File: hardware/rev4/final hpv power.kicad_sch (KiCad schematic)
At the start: 27 parts, among them J1 Conn_02x03_Odd_Even, J2 Conn_01x04_Pin, Q1 PNP, U1 ESP32-S3-MINI-1, U2 MCP1825S, U3 HX711

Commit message: fixed up things for justin to look
fixed up things for justin to look
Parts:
- removed J1: Conn_02x03_Odd_Even, Connector_IDC:IDC-Header_2x03_P2.54mm_Vertical, symbol Connector_Generic:Conn_02x03_Odd_Even
- added J3: USB_C_Receptacle_USB2.0_14P, Connector_USB:USB_C_Receptacle_GCT_USB4110, symbol Connector:USB_C_Receptacle_USB2.0_14P
- added R7, R8: 5.1k, Resistor_SMD:R_0805_2012Metric, symbol Device:R
- C1, C10, C11, C12, C2, C3, C4, C5, C6, C7, C8, C9: footprint Capacitor_SMD:C_0603_1608Metric -> Capacitor_SMD:C_0805_2012Metric
- D1, D2: footprint LED_SMD:LED_0603_1608Metric -> LED_SMD:LED_0805_2012Metric
- R1, R2, R3, R4, R5, R6: footprint Resistor_SMD:R_0603_1608Metric -> Resistor_SMD:R_0805_2012Metric
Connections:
- net BATT: no longer C5.2, U2.1 (VI)
- net GND: now also J3.A1 (GND), J3.A12 (GND), J3.B1 (GND), J3.B12 (GND), J3.S1 (SHIELD), R7.2, R8.2
- net D-: now reaches U1.23 (USB_D-)
- net D-: now also J3.A7 (D-), J3.B7 (D-)
- net D+: now reaches U1.24 (USB_D+)
- net D+: now also J3.A6 (D+), J3.B6 (D+)
- net RX: no longer names the net of U1.40 (RXD0)
- net TX: no longer names the net of U1.39 (TXD0)
- new net: J3.A5 (CC1), R7.1
- new net: J3.B5 (CC2), R8.1
- new net VBUS: C5.2, J3.A4 (VBUS), J3.A9 (VBUS), J3.B4 (VBUS), J3.B9 (VBUS), U2.1 (VI)
- no-connect marks 31 -> 29
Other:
- note removed: "Can look into an external analog digital converter, apparently the one in the mcu isnt very precise for the strain gauge signals we are reading"
- note removed: "Figure out bluetooth low energy, and battery"
- note removed: "Need to check pinouts for mcu Clear Errors Look into USBC"
- note removed: "Noah: battery should be pretty simple, connect to voltage reg according to datasheet bluetooth low energy is built into the MCU, we just have to code it with the right library"
- note removed: "Programming (ESP PROG)"
- note removed: "eason"

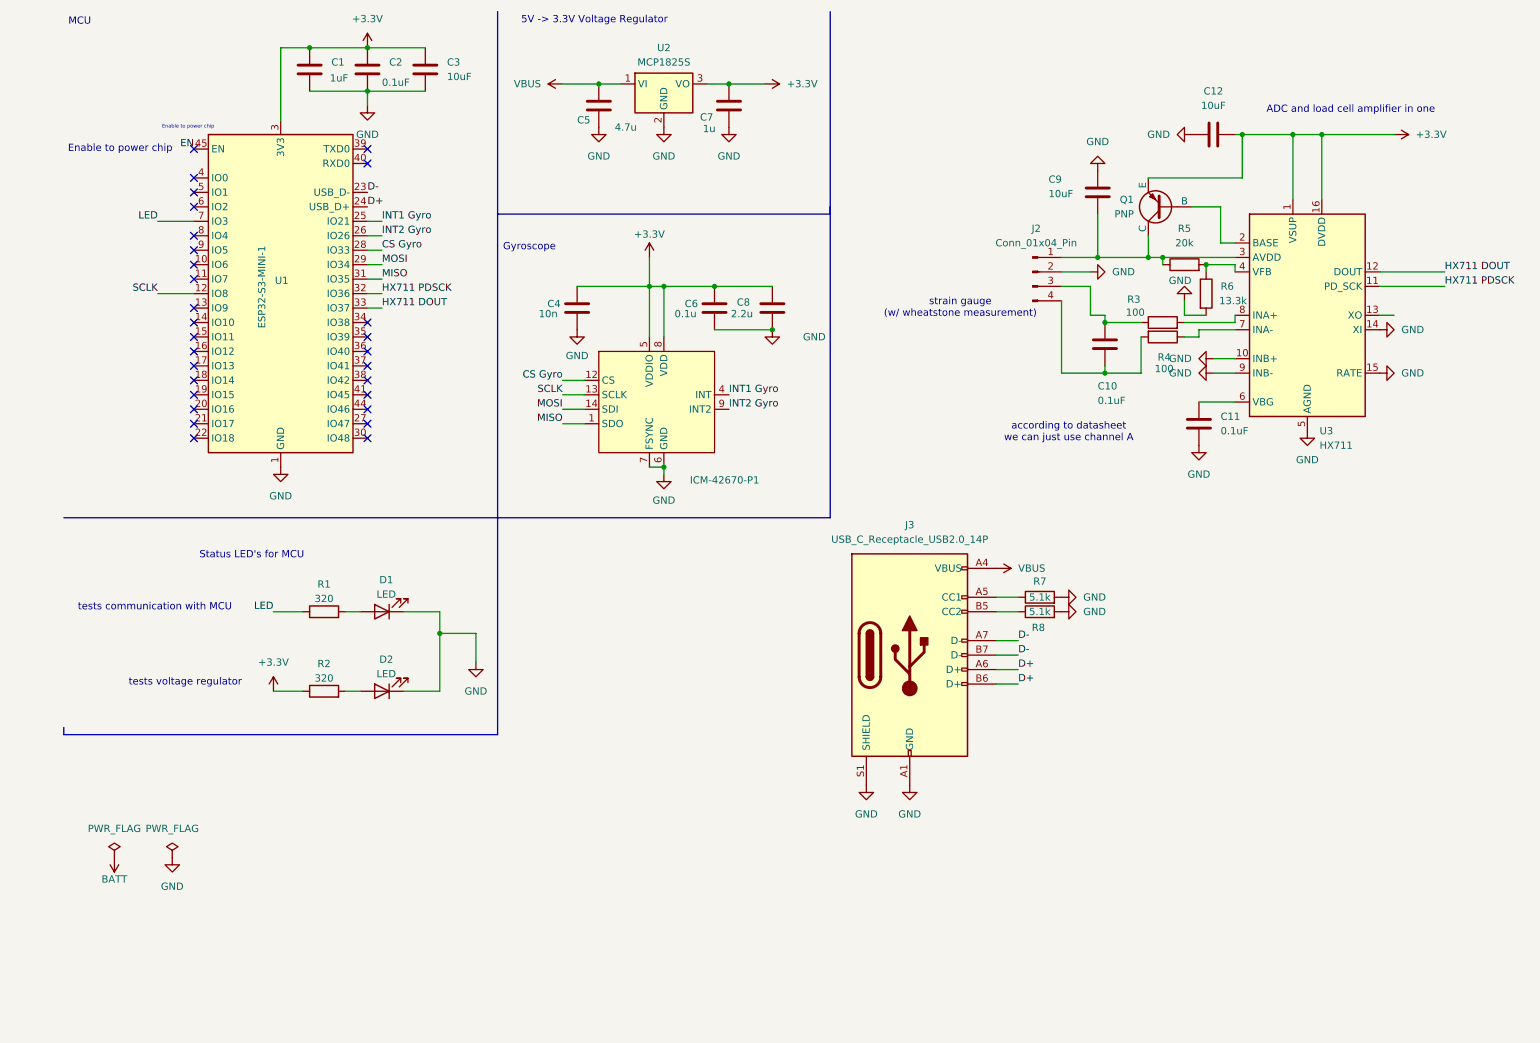
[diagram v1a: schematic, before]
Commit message: Fixed schematic based on Noah's notes from Justin
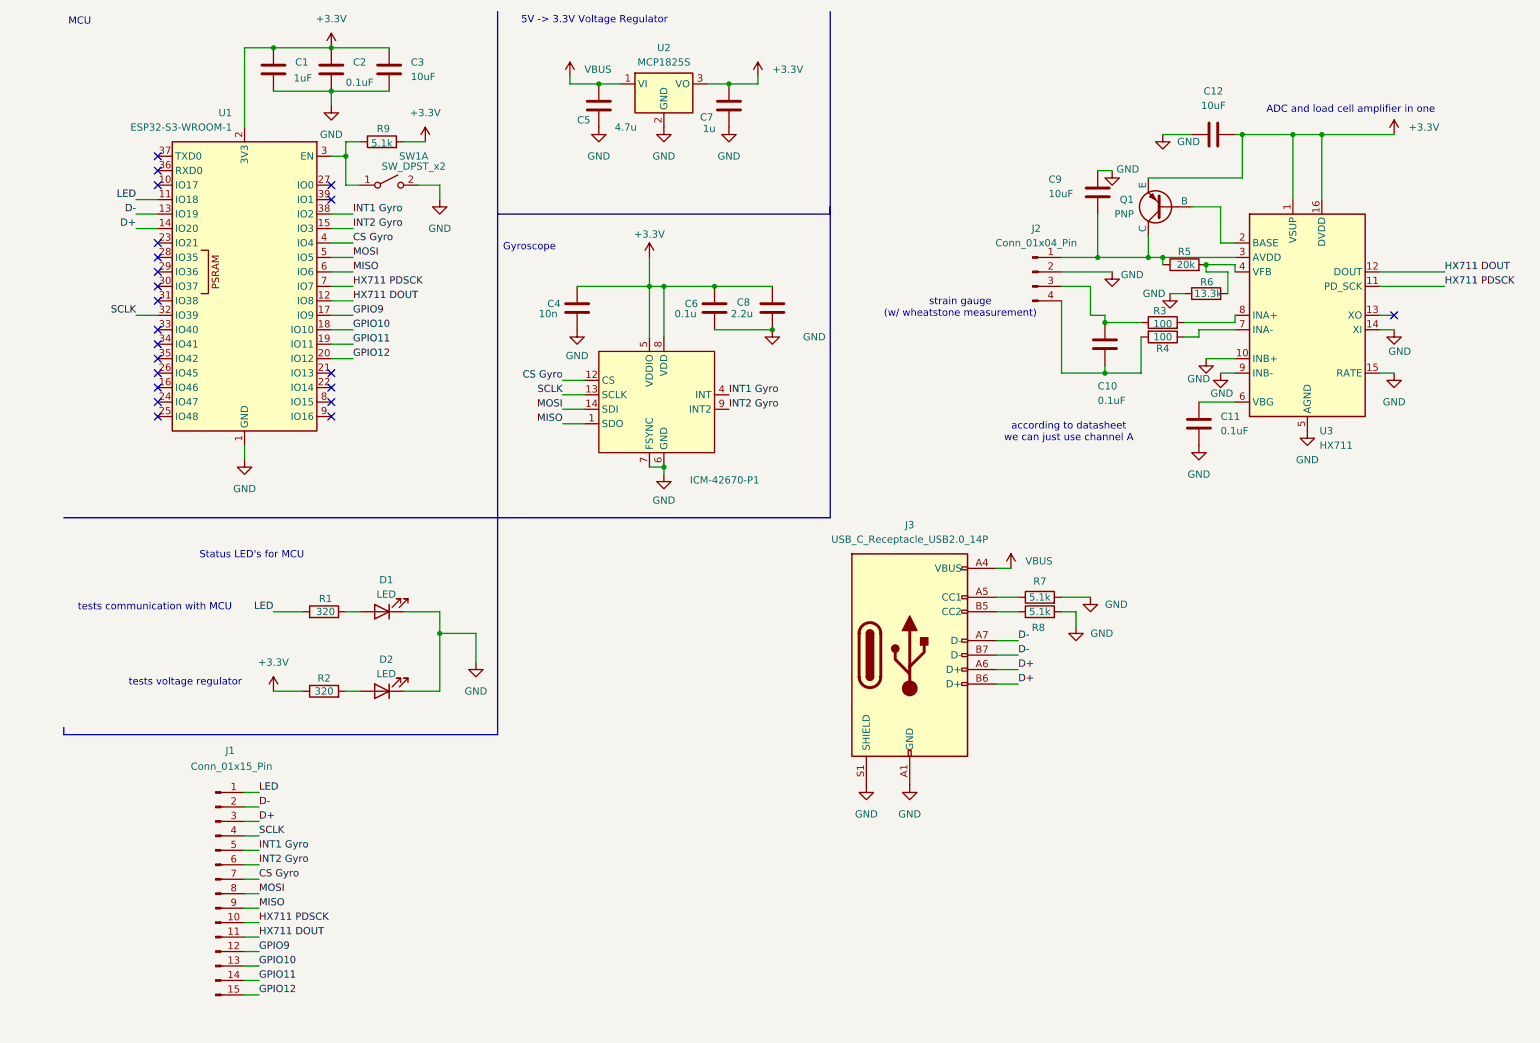
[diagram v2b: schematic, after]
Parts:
- removed U1: ESP32-S3-MINI-1, RF_Module:ESP32-S2-MINI-1, symbol RF_Module:ESP32-S3-MINI-1
- added J1: Conn_01x15_Pin, Connector_JST:JST_EH_S15B-EH_1x15_P2.50mm_Horizontal, symbol Connector:Conn_01x15_Pin
- added R9: 5.1k, Resistor_SMD:R_0805_2012Metric, symbol Device:R
- added SW1: SW_DPST_x2, Button_Switch_SMD:SW_DIP_SPSTx02_Slide_6.7x6.64mm_W6.73mm_P2.54mm_LowProfile_JPin, symbol Switch:SW_DPST_x2
- added U1: ESP32-S3-WROOM-1, RF_Module:ESP32-S3-WROOM-1, symbol RF_Module:ESP32-S3-WROOM-1
- C1, C12, C3, C5, C7, C8, C9: Digikey Link (none) -> https://www.digikey.ca/en/products/detail/samsung-electro-m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; Item Name (none) -> Capacitor
- C10, C11, C2, C6: Digikey Link (none) -> https://www.digikey.ca/en/products/detail/kemet/C0603C104K5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; Item Name (none) -> Capacitor
- C4: Digikey Link (none) -> https://www.digikey.ca/en/products/detail/kemet/C0603C103K5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; Item Name (none) -> Capacitor
- D1, D2: Digikey Link (none) -> https://www.digikey.ca/en/products/detail/w%C3%BCrth-elektr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; Item Name (none) -> LEDs
- ICM-42670-P1: Digikey Link (none) -> https://www.digikey.ca/en/products/detail/tdk-invensense/IC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; Item Name (none) -> Gyroscope
- J2: Digikey Link (none) -> https://www.digikey.ca/en/products/detail/jst-sales-america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; Item Name (none) -> Header
- J3: Item Name (none) -> USB C
- Q1: Digikey Link (none) -> https://www.digikey.ca/en/products/detail/mcc-micro-commerc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; Item Name (none) -> Transistor
- R1, R2: Digikey Link (none) -> https://www.digikey.ca/en/products/detail/koa-speer-electro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; Item Name (none) -> Resistor
- R3, R4, R5: Digikey Link (none) -> https://www.digikey.ca/en/products/detail/yageo/RC0603FR-07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; Item Name (none) -> Resistor
- R6: Digikey Link (none) -> https://www.digikey.ca/en/products/detail/stackpole-electro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; Item Name (none) -> Resistor
- R7, R8: Item Name (none) -> Resistor
- U2: Digikey Link (none) -> https://www.digikey.ca/en/products/detail/microchip-technol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; Item Name (none) -> Voltage Regulator
- U3: Digikey Link (none) -> https://www.digikey.ca/en/products/detail/sparkfun-electron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; Item Name (none) -> HX711
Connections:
- net +3.3V: now also R9.2, U1.2 (3V3)
- net CS Gyro: now also J1.7 (Pin_7), U1.4 (IO4)
- net D+: now also J1.3 (Pin_3), U1.14 (IO20)
- net D-: now also J1.2 (Pin_2), U1.13 (IO19)
- net GND: now also R6.1, SW1.2 (B), U1.1 (GND), U1.40 (GND), U1.41 (GND); no longer R6.2
- net HX711 DOUT: now also J1.11 (Pin_11), U1.12 (IO8)
- net HX711 PDSCK: now also J1.10 (Pin_10), U1.7 (IO7)
- net INT1 Gyro: now also J1.5 (Pin_5), U1.38 (IO2)
- net INT2 Gyro: now also J1.6 (Pin_6), U1.15 (IO3)
- net LED: now also J1.1 (Pin_1), U1.11 (IO18)
- net MISO: now also J1.9 (Pin_9), U1.6 (IO6)
- net MOSI: now also J1.8 (Pin_8), U1.5 (IO5)
- net SCLK: now also J1.4 (Pin_4), U1.32 (IO39)
- net at R5.2, U3.4 (VFB): now also R6.2; no longer R6.1
- new net: R9.1, SW1.1 (A), U1.3 (EN)
- new net GPIO10: J1.13 (Pin_13), U1.18 (IO10)
- new net GPIO11: J1.14 (Pin_14), U1.19 (IO11)
- new net GPIO12: J1.15 (Pin_15), U1.20 (IO12)
- new net GPIO9: J1.12 (Pin_12), U1.17 (IO9)
- no-connect marks 29 -> 22
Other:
- note removed: "Enable to power chip"
- moved on the sheet: C1, C2, C3, R6

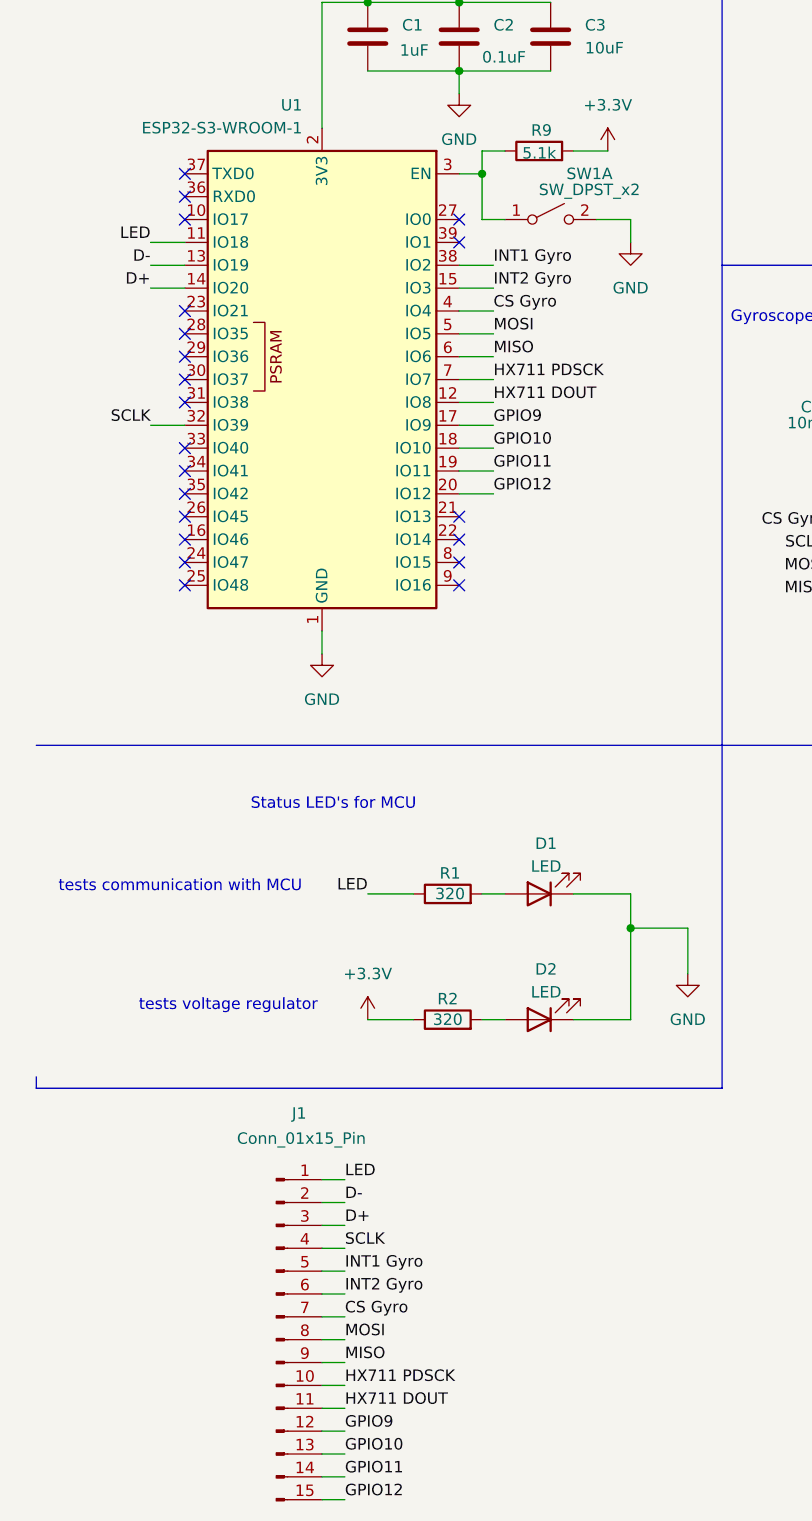
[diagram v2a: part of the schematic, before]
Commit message: Updated PCB and schematic for esp32 s3 wroom
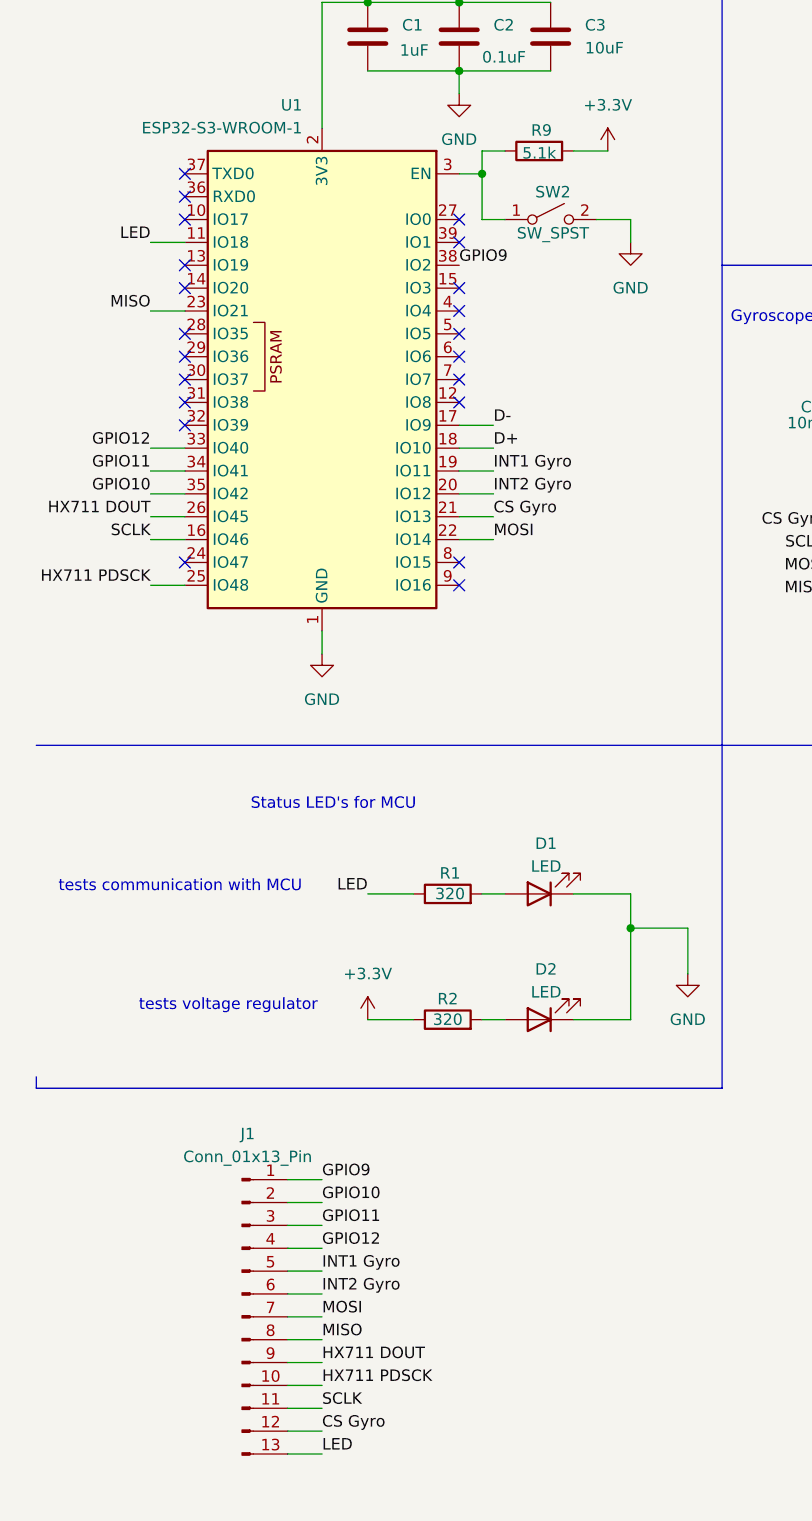
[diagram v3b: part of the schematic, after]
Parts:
- removed J1: Conn_01x15_Pin, Connector_JST:JST_EH_S15B-EH_1x15_P2.50mm_Horizontal, symbol Connector:Conn_01x15_Pin
- removed SW1: SW_DPST_x2, Button_Switch_SMD:SW_DIP_SPSTx02_Slide_6.7x6.64mm_W6.73mm_P2.54mm_LowProfile_JPin, symbol Switch:SW_DPST_x2
- added J1: Conn_01x13_Pin, Connector_JST:JST_EH_S13B-EH_1x13_P2.50mm_Horizontal, symbol Connector:Conn_01x13_Pin
- added SW2: SW_SPST, Button_Switch_SMD:SW_SPST_B3S-1000, symbol Switch:SW_SPST
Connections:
- net CS Gyro: now also U1.21 (IO13), J1.12 (Pin_12); no longer U1.4 (IO4)
- net D+: now also U1.18 (IO10); no longer U1.14 (IO20)
- net D-: now also U1.17 (IO9); no longer U1.13 (IO19)
- net GND: now also SW2.2 (B)
- net GPIO10: now also U1.35 (IO42), J1.2 (Pin_2); no longer U1.18 (IO10)
- net GPIO11: now also U1.34 (IO41), J1.3 (Pin_3); no longer U1.19 (IO11)
- net GPIO12: now also U1.33 (IO40), J1.4 (Pin_4); no longer U1.20 (IO12)
- net GPIO9: now also U1.38 (IO2), J1.1 (Pin_1); no longer U1.17 (IO9)
- net HX711 DOUT: now also U1.26 (IO45), J1.9 (Pin_9); no longer U1.12 (IO8)
- net HX711 PDSCK: now also U1.25 (IO48), J1.10 (Pin_10); no longer U1.7 (IO7)
- net INT1 Gyro: now also U1.19 (IO11), J1.5 (Pin_5); no longer U1.38 (IO2)
- net INT2 Gyro: now also U1.20 (IO12), J1.6 (Pin_6); no longer U1.15 (IO3)
- net LED: now also J1.13 (Pin_13)
- net MISO: now also U1.23 (IO21), J1.8 (Pin_8); no longer U1.6 (IO6)
- net MOSI: now also U1.22 (IO14), J1.7 (Pin_7); no longer U1.5 (IO5)
- net SCLK: now also U1.16 (IO46), J1.11 (Pin_11); no longer U1.32 (IO39)
- net at R9.1, U1.3 (EN): now also SW2.1 (A)

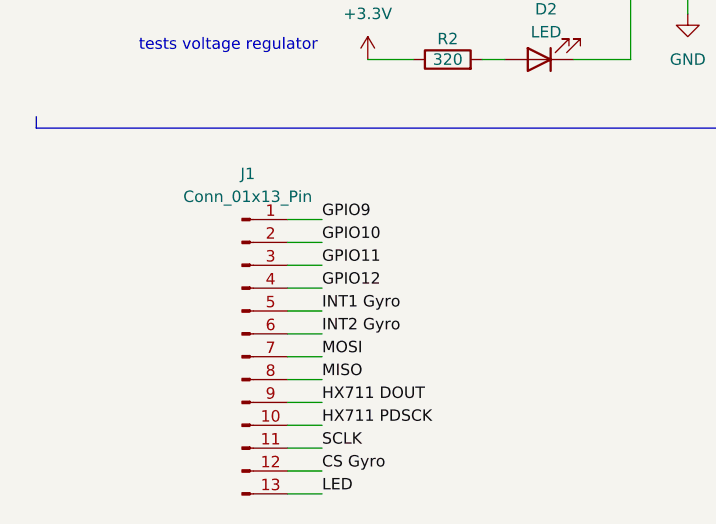
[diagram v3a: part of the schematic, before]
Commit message: Fixing up PCB
added pull up resistor, replaced esp footprint, added header
made are a lot smaller
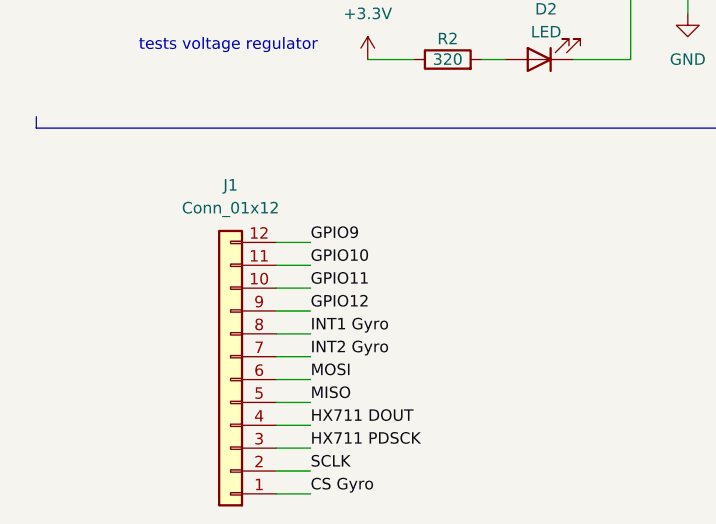
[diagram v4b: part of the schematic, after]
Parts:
- removed J1: Conn_01x13_Pin, Connector_JST:JST_EH_S13B-EH_1x13_P2.50mm_Horizontal, symbol Connector:Conn_01x13_Pin
- added J1: Conn_01x12, Connector_JST:JST_EH_B12B-EH-A_1x12_P2.50mm_Vertical, symbol Connector_Generic:Conn_01x12
- J2: footprint Connector_JST:JST_EH_S4B-EH_1x04_P2.50mm_Horizontal -> Connector_JST:JST_EH_B4B-EH-A_1x04_P2.50mm_Vertical
- SW2: footprint Button_Switch_SMD:SW_SPST_B3S-1000 -> Button_Switch_THT:SW_PUSH_6mm_H4.3mm
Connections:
- net CS Gyro: now also J1.1 (Pin_1)
- net GPIO10: now also J1.11 (Pin_11)
- net GPIO11: now also J1.10 (Pin_10)
- net GPIO12: now also J1.9 (Pin_9)
- net GPIO9: now also J1.12 (Pin_12)
- net HX711 DOUT: now also J1.4 (Pin_4)
- net HX711 PDSCK: now also J1.3 (Pin_3)
- net INT1 Gyro: now also J1.8 (Pin_8)
- net INT2 Gyro: now also J1.7 (Pin_7)
- net MISO: now also J1.5 (Pin_5)
- net MOSI: now also J1.6 (Pin_6)
- net SCLK: now also J1.2 (Pin_2)
